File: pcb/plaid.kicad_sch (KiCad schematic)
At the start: 130 parts, among them J2 AVR_ISP_6, J3 Conn_01x04, SW1 SW_Push, SW10 SW_Push, SW11 SW_Push, SW12 SW_Push, SW13 SW_Push, SW14 SW_Push, SW15 SW_Push, SW16 SW_Push, SW17 SW_Push, SW18 SW_Push, SW19 SW_Push, SW2 SW_Push, SW20 SW_Push, SW21 SW_Push, SW22 SW_Push, SW23 SW_Push, SW24 SW_Push, SW25 SW_Push, SW26 SW_Push, SW27 SW_Push, SW28 SW_Push, SW29 SW_Push, SW3 SW_Push, SW30 SW_Push, SW31 SW_Push, SW32 SW_Push, SW33 SW_Push, SW34 SW_Push, SW35 SW_Push, SW36 SW_Push, SW37 SW_Push, SW38 SW_Push, SW39 SW_Push, SW4 SW_Push, SW40 SW_Push, SW41 SW_Push, SW42 SW_Push, SW43 SW_Push, SW44 SW_Push, SW45 SW_Push, SW46 SW_Push, SW47 SW_Push, SW48 SW_Push, SW49 SW_Push, SW5 SW_Push, SW50 RESET, SW51 BOOT, SW6 SW_Push, SW7 SW_Push, SW8 SW_Push, SW9 SW_Push, U1 ATMEGA328-PU, Y1 16MHz

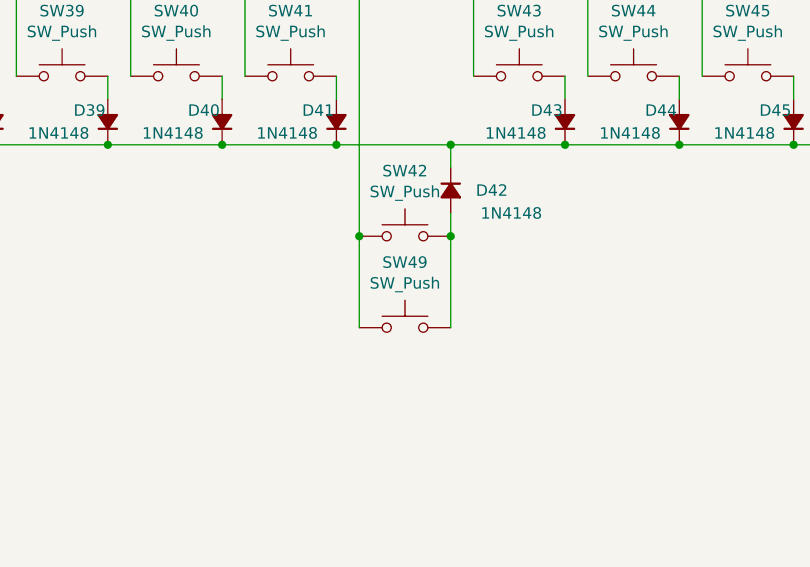
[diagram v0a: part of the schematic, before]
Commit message: Add support for Kailh Choc switches
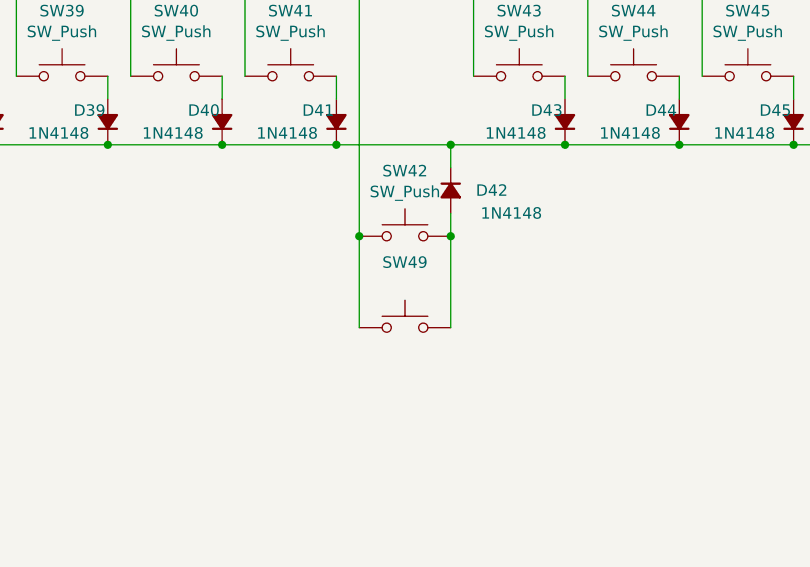
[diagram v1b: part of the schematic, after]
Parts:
- SW1, SW10, SW11, SW12, SW13, SW14, SW15, SW16, SW17, SW18, SW19, SW2, SW20, SW21, SW22, SW23, SW24, SW25, SW26, SW27, SW28, SW29, SW3, SW30, SW31, SW32, SW33, SW34, SW35, SW36, SW37, SW38, SW39, SW4, SW40, SW41, SW42, SW43, SW44, SW45, SW46, SW47, SW48, SW5, SW6, SW7, SW8, SW9: footprint SMKJP:SW_Cherry_MX1A_1.00u_PCB -> (none)
- SW49: value SW_Push -> (none); footprint SMKJP:SW_Cherry_MX1A_2.0U_PCB_universal_center -> (none)

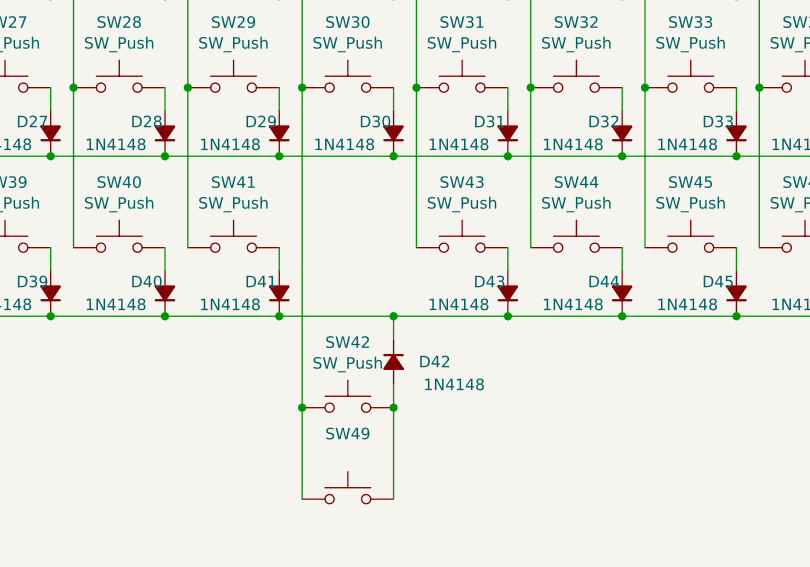
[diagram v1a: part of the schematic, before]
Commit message: Fix spacebar(s) - use "opposing" footprints
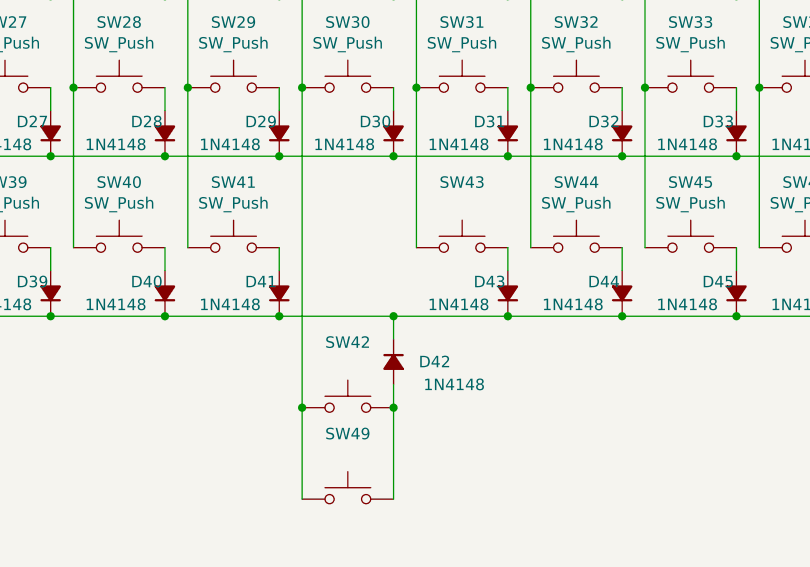
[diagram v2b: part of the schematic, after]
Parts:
- SW1, SW10, SW11, SW12, SW13, SW14, SW15, SW16, SW17, SW18, SW19, SW2, SW20, SW21, SW22, SW23, SW24, SW25, SW26, SW27, SW28, SW29, SW3, SW30, SW31, SW32, SW33, SW34, SW35, SW36, SW37, SW38, SW39, SW4, SW40, SW41, SW44, SW45, SW46, SW47, SW48, SW5, SW6, SW7, SW8, SW9: footprint (none) -> 42keebs:MX-Choc-1U-NoLED
- SW42, SW43: value SW_Push -> (none)
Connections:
- net COL6: now also SW43.2; no longer SW43.1
- net at D43.2 (A): now also SW43.1; no longer SW43.2
